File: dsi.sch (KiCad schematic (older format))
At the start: 18 parts, among them J1201 Touch, J1202 LCD, Q1201 2SK3018, Q1202 2SK3018

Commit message: added footprint for display FPC connector
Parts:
- J1202: footprint (none) -> dvk-mx8m-bsb:Conn_Hirose_FPC_39x0_3
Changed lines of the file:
@@
 F 0 "J1202" H 9650 5150 50  0000 C CNN
 F 1 "LCD" H 9650 1150 50  0000 C CNN
-F 2 "" H 9650 3150 50  0001 C CNN
+F 2 "dvk-mx8m-bsb:Conn_Hirose_FPC_39x0_3" H 9650 3150 50  0001 C CNN
 F 3 "https://www.hirose.com/product/en/download_file/key_name/FH26-39S-0.3SHW%2805%29/category/Drawing%20(2D)/doc_file_id/42931/?file_category_id=6&item_id=05800201105&is_series=" H 9650 3150 50  0001 C CNN
 F 4 "Hirose" H 9650 3150 60  0001 C CNN "MFG Name"
@@
 $Bitmap
 Pos 10000 5700
-Scale 1.000000
+Scale 1,000000
 Data
 89 50 4E 47 0D 0A 1A 0A 00 00 00 0D 49 48 44 52 00 00 01 71 00 00 00 44 08 02 00 00 00 F8 25 92
@@
 $Bitmap
 Pos 5200 4500
-Scale 1.000000
+Scale 1,000000
 Data
 89 50 4E 47 0D 0A 1A 0A 00 00 00 0D 49 48 44 52 00 00 00 C1 00 00 00 F5 08 02 00 00 00 66 CB 06
@@
 $Bitmap
 Pos 5350 5175
-Scale 1.000000
+Scale 1,000000
 Data
 89 50 4E 47 0D 0A 1A 0A 00 00 00 0D 49 48 44 52 00 00 00 5C 00 00 00 67 08 02 00 00 00 02 30 B2
@@
 $Bitmap
 Pos 5000 5150
-Scale 1.000000
+Scale 1,000000
 Data
 89 50 4E 47 0D 0A 1A 0A 00 00 00 0D 49 48 44 52 00 00 00 4D 00 00 00 5B 08 02 00 00 00 B9 E4 9F
@@
 $Bitmap
 Pos 10100 5000
-Scale 1.000000
+Scale 1,000000
 Data
 89 50 4E 47 0D 0A 1A 0A 00 00 00 0D 49 48 44 52 00 00 00 46 00 00 00 99 08 02 00 00 00 1D 24 DB
@@
 $Bitmap
 Pos 10500 5000
-Scale 1.000000
+Scale 1,000000
 Data
 89 50 4E 47 0D 0A 1A 0A 00 00 00 0D 49 48 44 52 00 00 00 5A 00 00 00 96 08 02 00 00 00 D1 E0 08

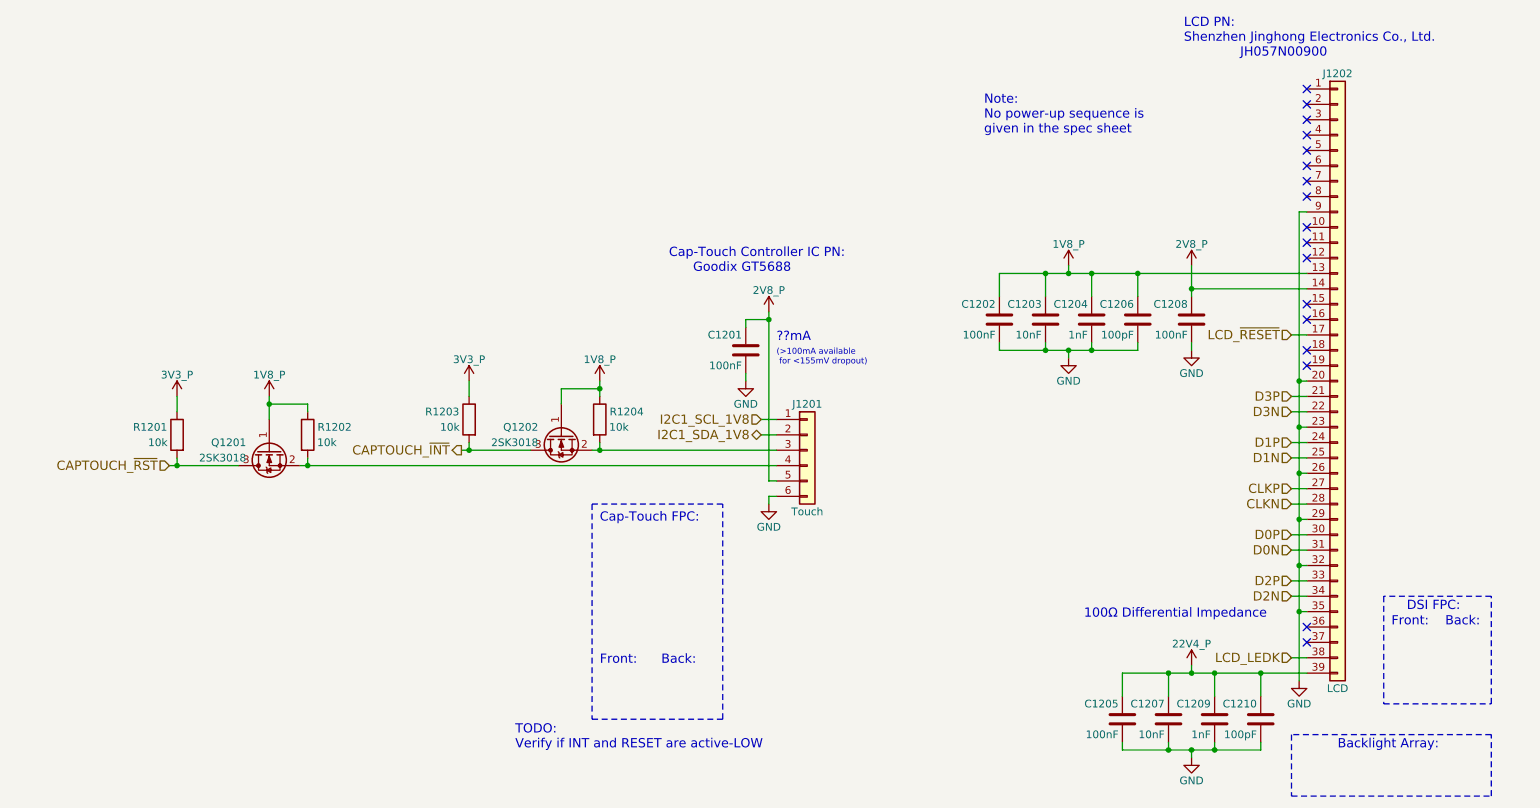
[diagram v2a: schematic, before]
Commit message: Include address in schematic notes for all I2C1 slaves, make HDMI connector shielding resistor to GND 0Ohms
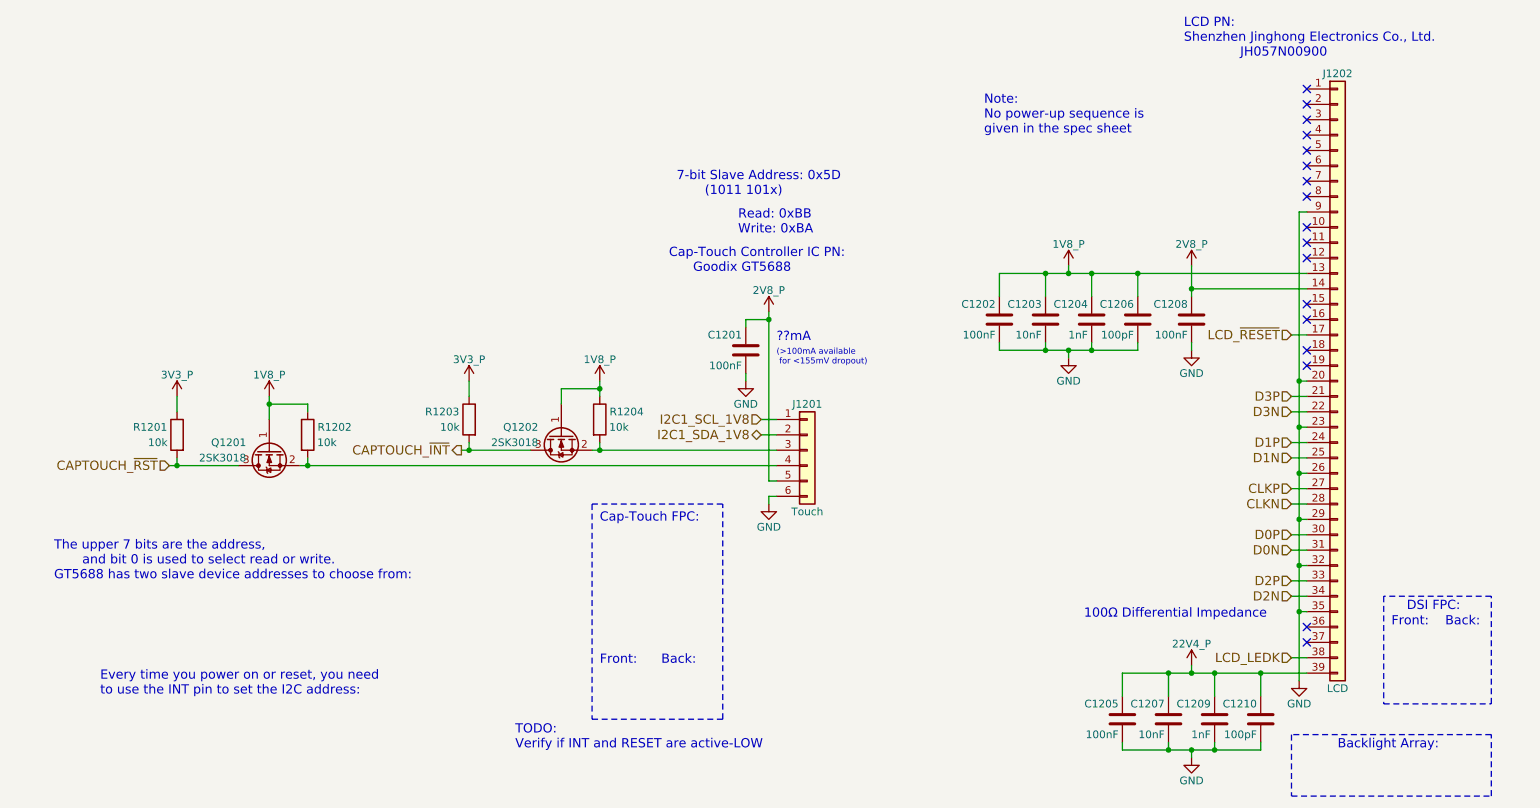
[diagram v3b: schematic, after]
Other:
- note added: "7-bit Slave Address: 0x5D\n (1011 101x)"
- note added: "Every time you power on or reset, you need\nto use the INT pin to set the I2C address:"
- note added: "Read: 0xBB\nWrite: 0xBA"
- note added: "The upper 7 bits are the address,\n and bit 0 is used to select read or write.\nGT5688 has two slave device addresses to choose from:"

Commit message: Assign most of the capacitors their respective footprints (most are 0603s), add camera/CSI connector component info, source cheaper distributors for 3.5mm headset jack and RJ45
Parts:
- C1201, C1202, C1203, C1204, C1205, C1206, C1207, C1208, C1209, C1210: footprint (none) -> Capacitors_SMD:C_0603
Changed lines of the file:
@@
 Note:\nNo power-up sequence is\ngiven in the spec sheet
 $Comp
-L 3V3_P #PWR1203
+L 3V3_P #PWR0180
 U 1 1 5AEA3227
 P 4000 3150
-F 0 "#PWR1203" H 4000 3000 50  0001 C CNN
+F 0 "#PWR0180" H 4000 3000 50  0001 C CNN
 F 1 "3V3_P" H 4000 3290 50  0000 C CNN
 F 2 "" H 4000 3150 50  0001 C CNN
@@
 $EndComp
 $Comp
-L 3V3_P #PWR1201
+L 3V3_P #PWR0181
 U 1 1 5AEA329B
 P 2100 3250
-F 0 "#PWR1201" H 2100 3100 50  0001 C CNN
+F 0 "#PWR0181" H 2100 3100 50  0001 C CNN
 F 1 "3V3_P" H 2100 3390 50  0000 C CNN
 F 2 "" H 2100 3250 50  0001 C CNN
@@
 $EndComp
 $Comp
-L 1V8_P #PWR1202
+L 1V8_P #PWR0182
 U 1 1 5AEDE2F3
 P 2700 3250
-F 0 "#PWR1202" H 2700 3100 50  0001 C CNN
+F 0 "#PWR0182" H 2700 3100 50  0001 C CNN
 F 1 "1V8_P" H 2700 3390 50  0000 C CNN
 F 2 "" H 2700 3250 50  0001 C CNN
@@
 $EndComp
 $Comp
-L 1V8_P #PWR1204
+L 1V8_P #PWR0183
 U 1 1 5B300B10
 P 4850 3150
-F 0 "#PWR1204" H 4850 3000 50  0001 C CNN
+F 0 "#PWR0183" H 4850 3000 50  0001 C CNN
 F 1 "1V8_P" H 4850 3290 50  0000 C CNN
 F 2 "" H 4850 3150 50  0001 C CNN
@@
 $EndComp
 $Comp
-L GND #PWR1214
+L GND #PWR0184
 U 1 1 5B314AC6
 P 9400 5100
-F 0 "#PWR1214" H 9400 4850 50  0001 C CNN
+F 0 "#PWR0184" H 9400 4850 50  0001 C CNN
 F 1 "GND" H 9400 4950 50  0000 C CNN
 F 2 "" H 9400 5100 50  0001 C CNN
@@
 NoConn ~ 9450 4850
 $Comp
-L 22V4_P #PWR1212
+L 22V4_P #PWR0185
 U 1 1 5B3239F0
 P 8700 5000
-F 0 "#PWR1212" H 8700 4850 50  0001 C CNN
+F 0 "#PWR0185" H 8700 4850 50  0001 C CNN
 F 1 "22V4_P" H 8700 5140 50  0000 C CNN
 F 2 "" H 8700 5000 50  0001 C CNN
@@
 NoConn ~ 9450 2950
 $Comp
-L 1V8_P #PWR1208
+L 1V8_P #PWR0186
 U 1 1 5B328FC1
 P 7900 2400
-F 0 "#PWR1208" H 7900 2250 50  0001 C CNN
+F 0 "#PWR0186" H 7900 2250 50  0001 C CNN
 F 1 "1V8_P" H 7900 2540 50  0000 C CNN
 F 2 "" H 7900 2400 50  0001 C CNN
@@
 F 0 "C1202" H 7475 2850 50  0000 L CNN
 F 1 "100nF" H 7475 2650 50  0000 L CNN
-F 2 "" H 7488 2600 50  0001 C CNN
+F 2 "Capacitors_SMD:C_0603" H 7488 2600 50  0001 C CNN
 F 3 "" H 7450 2750 50  0001 C CNN
 	1    7450 2750
@@
 $EndComp
 $Comp
-L GND #PWR1209
+L GND #PWR0187
 U 1 1 5B32A2F2
 P 7900 3000
-F 0 "#PWR1209" H 7900 2750 50  0001 C CNN
+F 0 "#PWR0187" H 7900 2750 50  0001 C CNN
 F 1 "GND" H 7900 2850 50  0000 C CNN
 F 2 "" H 7900 3000 50  0001 C CNN
@@
 	9350 4550 9450 4550
 $Comp
-L 2V8_P #PWR1210
+L 2V8_P #PWR0188
 U 1 1 5B3FFD6E
 P 8700 2400
-F 0 "#PWR1210" H 8700 2250 50  0001 C CNN
+F 0 "#PWR0188" H 8700 2250 50  0001 C CNN
 F 1 "2V8_P" H 8700 2540 50  0000 C CNN
 F 2 "" H 8700 2400 50  0001 C CNN
@@
 F 0 "C1208" H 8725 2850 50  0000 L CNN
 F 1 "100nF" H 8725 2650 50  0000 L CNN
-F 2 "" H 8738 2600 50  0001 C CNN
+F 2 "Capacitors_SMD:C_0603" H 8738 2600 50  0001 C CNN
 F 3 "" H 8700 2750 50  0001 C CNN
 	1    8700 2750
@@
 $EndComp
 $Comp
-L GND #PWR1211
+L GND #PWR0189
 U 1 1 5B3FFE19
 P 8700 2950
-F 0 "#PWR1211" H 8700 2700 50  0001 C CNN
+F 0 "#PWR0189" H 8700 2700 50  0001 C CNN
 F 1 "GND" H 8700 2800 50  0000 C CNN
 F 2 "" H 8700 2950 50  0001 C CNN
@@
 	5900 3500 6000 3500
 $Comp
-L GND #PWR1207
+L GND #PWR0190
 U 1 1 5B449295
 P 5950 3950
-F 0 "#PWR1207" H 5950 3700 50  0001 C CNN
+F 0 "#PWR0190" H 5950 3700 50  0001 C CNN
 F 1 "GND" H 5950 3800 50  0000 C CNN
 F 2 "" H 5950 3950 50  0001 C CNN
@@
 	5950 2700 5950 3800
 $Comp
-L 2V8_P #PWR1206
+L 2V8_P #PWR0191
 U 1 1 5B449772
 P 5950 2700
-F 0 "#PWR1206" H 5950 2550 50  0001 C CNN
+F 0 "#PWR0191" H 5950 2550 50  0001 C CNN
 F 1 "2V8_P" H 5950 2840 50  0000 C CNN
 F 2 "" H 5950 2700 50  0001 C CNN
@@
 F 0 "C1201" H 5825 3050 50  0000 L CNN
 F 1 "100nF" H 5825 2850 50  0000 L CNN
-F 2 "" H 5838 2800 50  0001 C CNN
+F 2 "Capacitors_SMD:C_0603" H 5838 2800 50  0001 C CNN
 F 3 "" H 5800 2950 50  0001 C CNN
 	1    5800 2950
@@
 $EndComp
 $Comp
-L GND #PWR1205
+L GND #PWR0192
 U 1 1 5B44A063
 P 5800 3150
-F 0 "#PWR1205" H 5800 2900 50  0001 C CNN
+F 0 "#PWR0192" H 5800 2900 50  0001 C CNN
 F 1 "GND" H 5800 3000 50  0000 C CNN
 F 2 "" H 5800 3150 50  0001 C CNN
@@
 F 0 "C1206" H 8375 2850 50  0000 L CNN
 F 1 "100pF" H 8375 2650 50  0000 L CNN
-F 2 "" H 8388 2600 50  0001 C CNN
+F 2 "Capacitors_SMD:C_0603" H 8388 2600 50  0001 C CNN
 F 3 "" H 8350 2750 50  0001 C CNN
 	1    8350 2750
@@
 F 0 "C1204" H 8075 2850 50  0000 L CNN
 F 1 "1nF" H 8075 2650 50  0000 L CNN
-F 2 "" H 8088 2600 50  0001 C CNN
+F 2 "Capacitors_SMD:C_0603" H 8088 2600 50  0001 C CNN
 F 3 "" H 8050 2750 50  0001 C CNN
 	1    8050 2750
@@
 F 0 "C1203" H 7775 2850 50  0000 L CNN
 F 1 "10nF" H 7775 2650 50  0000 L CNN
-F 2 "" H 7788 2600 50  0001 C CNN
+F 2 "Capacitors_SMD:C_0603" H 7788 2600 50  0001 C CNN
 F 3 "" H 7750 2750 50  0001 C CNN
 	1    7750 2750
@@
 F 0 "C1205" H 8275 5450 50  0000 L CNN
 F 1 "100nF" H 8275 5250 50  0000 L CNN
-F 2 "" H 8288 5200 50  0001 C CNN
+F 2 "Capacitors_SMD:C_0603" H 8288 5200 50  0001 C CNN
 F 3 "" H 8250 5350 50  0001 C CNN
 	1    8250 5350
@@
 $EndComp
 $Comp
-L GND #PWR1213
+L GND #PWR0193
 U 1 1 5B45292C
 P 8700 5600
-F 0 "#PWR1213" H 8700 5350 50  0001 C CNN
+F 0 "#PWR0193" H 8700 5350 50  0001 C CNN
 F 1 "GND" H 8700 5450 50  0000 C CNN
 F 2 "" H 8700 5600 50  0001 C CNN
@@
 F 0 "C1210" H 9175 5450 50  0000 L CNN
 F 1 "100pF" H 9175 5250 50  0000 L CNN
-F 2 "" H 9188 5200 50  0001 C CNN
+F 2 "Capacitors_SMD:C_0603" H 9188 5200 50  0001 C CNN
 F 3 "" H 9150 5350 50  0001 C CNN
 	1    9150 5350
@@
 F 0 "C1209" H 8875 5450 50  0000 L CNN
 F 1 "1nF" H 8875 5250 50  0000 L CNN
-F 2 "" H 8888 5200 50  0001 C CNN
+F 2 "Capacitors_SMD:C_0603" H 8888 5200 50  0001 C CNN
 F 3 "" H 8850 5350 50  0001 C CNN
 	1    8850 5350
@@
 F 0 "C1207" H 8575 5450 50  0000 L CNN
 F 1 "10nF" H 8575 5250 50  0000 L CNN
-F 2 "" H 8588 5200 50  0001 C CNN
+F 2 "Capacitors_SMD:C_0603" H 8588 5200 50  0001 C CNN
 F 3 "" H 8550 5350 50  0001 C CNN
 	1    8550 5350

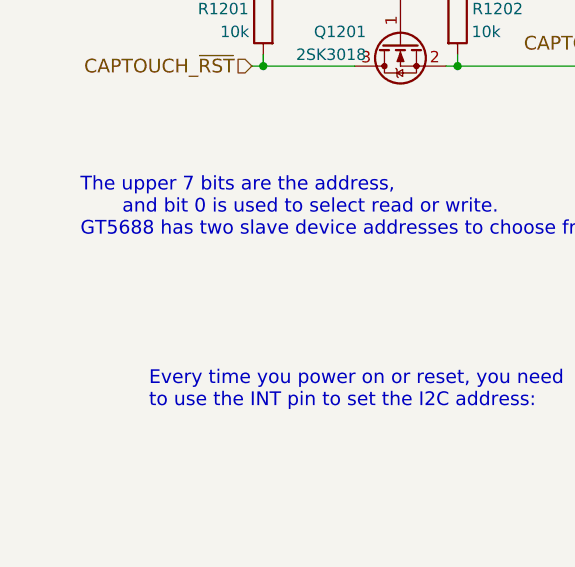
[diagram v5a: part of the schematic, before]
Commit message: Make corrections to schematic based on Emcraft's baseboard revision changes
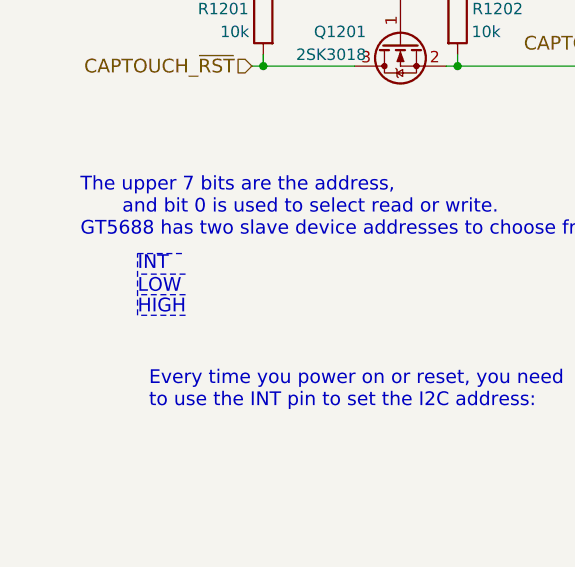
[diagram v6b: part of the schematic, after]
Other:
- note added: "HIGH"
- note added: "INT"
- note added: "LOW"
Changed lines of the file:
@@
 Sheet 12 24
 Title "MIPI DSI"
-Date "2018-05-31"
+Date "2018-06-01"
 Rev "v0.1.0"
 Comp "Purism SPC"
@@
 Note:\nNo power-up sequence is\ngiven in the spec sheet
 $Comp
-L 3V3_P #PWR0180
+L 3V3_P #PWR0182
 U 1 1 5AEA3227
 P 4000 3150
-F 0 "#PWR0180" H 4000 3000 50  0001 C CNN
+F 0 "#PWR0182" H 4000 3000 50  0001 C CNN
 F 1 "3V3_P" H 4000 3290 50  0000 C CNN
 F 2 "" H 4000 3150 50  0001 C CNN
@@
 $EndComp
 $Comp
-L 3V3_P #PWR0181
+L 3V3_P #PWR0183
 U 1 1 5AEA329B
 P 2100 3250
-F 0 "#PWR0181" H 2100 3100 50  0001 C CNN
+F 0 "#PWR0183" H 2100 3100 50  0001 C CNN
 F 1 "3V3_P" H 2100 3390 50  0000 C CNN
 F 2 "" H 2100 3250 50  0001 C CNN
@@
 $EndComp
 $Comp
-L 1V8_P #PWR0182
+L 1V8_P #PWR0184
 U 1 1 5AEDE2F3
 P 2700 3250
-F 0 "#PWR0182" H 2700 3100 50  0001 C CNN
+F 0 "#PWR0184" H 2700 3100 50  0001 C CNN
 F 1 "1V8_P" H 2700 3390 50  0000 C CNN
 F 2 "" H 2700 3250 50  0001 C CNN
@@
 $EndComp
 $Comp
-L 1V8_P #PWR0183
+L 1V8_P #PWR0185
 U 1 1 5B300B10
 P 4850 3150
-F 0 "#PWR0183" H 4850 3000 50  0001 C CNN
+F 0 "#PWR0185" H 4850 3000 50  0001 C CNN
 F 1 "1V8_P" H 4850 3290 50  0000 C CNN
 F 2 "" H 4850 3150 50  0001 C CNN
@@
 $EndComp
 $Comp
-L GND #PWR0184
+L GND #PWR0186
 U 1 1 5B314AC6
 P 9400 5100
-F 0 "#PWR0184" H 9400 4850 50  0001 C CNN
+F 0 "#PWR0186" H 9400 4850 50  0001 C CNN
 F 1 "GND" H 9400 4950 50  0000 C CNN
 F 2 "" H 9400 5100 50  0001 C CNN
@@
 NoConn ~ 9450 4850
 $Comp
-L 22V4_P #PWR0185
+L 22V4_P #PWR0187
 U 1 1 5B3239F0
 P 8700 5000
-F 0 "#PWR0185" H 8700 4850 50  0001 C CNN
+F 0 "#PWR0187" H 8700 4850 50  0001 C CNN
 F 1 "22V4_P" H 8700 5140 50  0000 C CNN
 F 2 "" H 8700 5000 50  0001 C CNN
@@
 NoConn ~ 9450 2950
 $Comp
-L 1V8_P #PWR0186
+L 1V8_P #PWR0188
 U 1 1 5B328FC1
 P 7900 2400
-F 0 "#PWR0186" H 7900 2250 50  0001 C CNN
+F 0 "#PWR0188" H 7900 2250 50  0001 C CNN
 F 1 "1V8_P" H 7900 2540 50  0000 C CNN
 F 2 "" H 7900 2400 50  0001 C CNN
@@
 $EndComp
 $Comp
-L GND #PWR0187
+L GND #PWR0189
 U 1 1 5B32A2F2
 P 7900 3000
-F 0 "#PWR0187" H 7900 2750 50  0001 C CNN
+F 0 "#PWR0189" H 7900 2750 50  0001 C CNN
 F 1 "GND" H 7900 2850 50  0000 C CNN
 F 2 "" H 7900 3000 50  0001 C CNN
@@
 	9350 4550 9450 4550
 $Comp
-L 2V8_P #PWR0188
+L 2V8_P #PWR0190
 U 1 1 5B3FFD6E
 P 8700 2400
-F 0 "#PWR0188" H 8700 2250 50  0001 C CNN
+F 0 "#PWR0190" H 8700 2250 50  0001 C CNN
 F 1 "2V8_P" H 8700 2540 50  0000 C CNN
 F 2 "" H 8700 2400 50  0001 C CNN
@@
 $EndComp
 $Comp
-L GND #PWR0189
+L GND #PWR0191
 U 1 1 5B3FFE19
 P 8700 2950
-F 0 "#PWR0189" H 8700 2700 50  0001 C CNN
+F 0 "#PWR0191" H 8700 2700 50  0001 C CNN
 F 1 "GND" H 8700 2800 50  0000 C CNN
 F 2 "" H 8700 2950 50  0001 C CNN
@@
 	5900 3500 6000 3500
 $Comp
-L GND #PWR0190
+L GND #PWR0192
 U 1 1 5B449295
 P 5950 3950
-F 0 "#PWR0190" H 5950 3700 50  0001 C CNN
+F 0 "#PWR0192" H 5950 3700 50  0001 C CNN
 F 1 "GND" H 5950 3800 50  0000 C CNN
 F 2 "" H 5950 3950 50  0001 C CNN
@@
 	5950 2700 5950 3800
 $Comp
-L 2V8_P #PWR0191
+L 2V8_P #PWR0193
 U 1 1 5B449772
 P 5950 2700
-F 0 "#PWR0191" H 5950 2550 50  0001 C CNN
+F 0 "#PWR0193" H 5950 2550 50  0001 C CNN
 F 1 "2V8_P" H 5950 2840 50  0000 C CNN
 F 2 "" H 5950 2700 50  0001 C CNN
@@
 $EndComp
 $Comp
-L GND #PWR0192
+L GND #PWR0194
 U 1 1 5B44A063
 P 5800 3150
-F 0 "#PWR0192" H 5800 2900 50  0001 C CNN
+F 0 "#PWR0194" H 5800 2900 50  0001 C CNN
 F 1 "GND" H 5800 3000 50  0000 C CNN
 F 2 "" H 5800 3150 50  0001 C CNN
@@
 $EndComp
 $Comp
-L GND #PWR0193
+L GND #PWR0195
 U 1 1 5B45292C
 P 8700 5600
-F 0 "#PWR0193" H 8700 5350 50  0001 C CNN
+F 0 "#PWR0195" H 8700 5350 50  0001 C CNN
 F 1 "GND" H 8700 5450 50  0000 C CNN
 F 2 "" H 8700 5600 50  0001 C CNN
@@
 Text Notes 5750 2200 0    60   ~ 0
 Read: 0xBB\nWrite: 0xBA
+Text Notes 1550 4700 0    60   ~ 0
+LOW
+Wire Notes Line
+	1760 4790 1550 4790
+Wire Notes Line
+	1550 4790 1550 4520
+Wire Notes Line
+	1760 4700 1550 4700
+Wire Notes Line
+	1550 4520 1760 4520
+Wire Notes Line
+	1760 4610 1550 4610
+Text Notes 1550 4600 0    60   ~ 0
+INT
+Text Notes 1550 4790 0    60   ~ 0
+HIGH
 $EndSCHEMATC
